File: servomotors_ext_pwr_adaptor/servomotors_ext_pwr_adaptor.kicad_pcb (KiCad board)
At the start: 2 copper layers, 2 parts

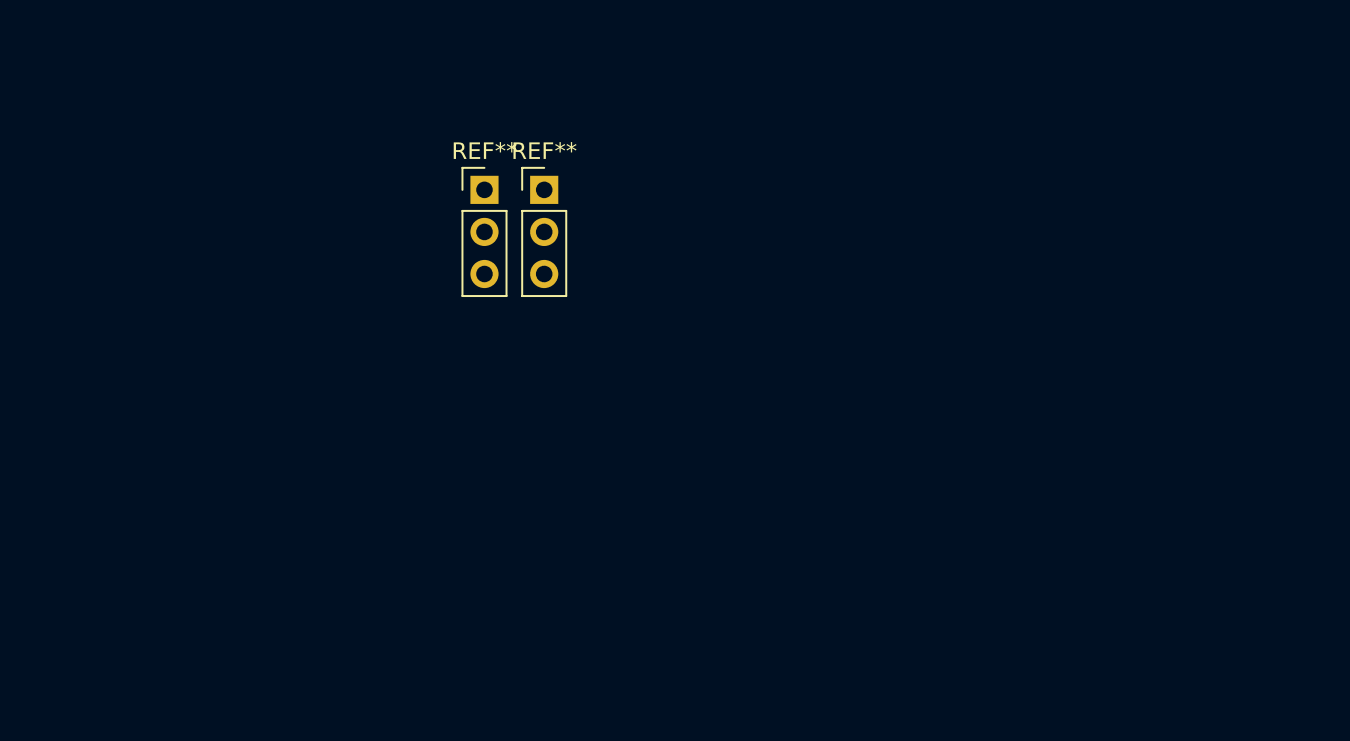
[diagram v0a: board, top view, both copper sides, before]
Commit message: Schematic done. Symbols and footrpints added
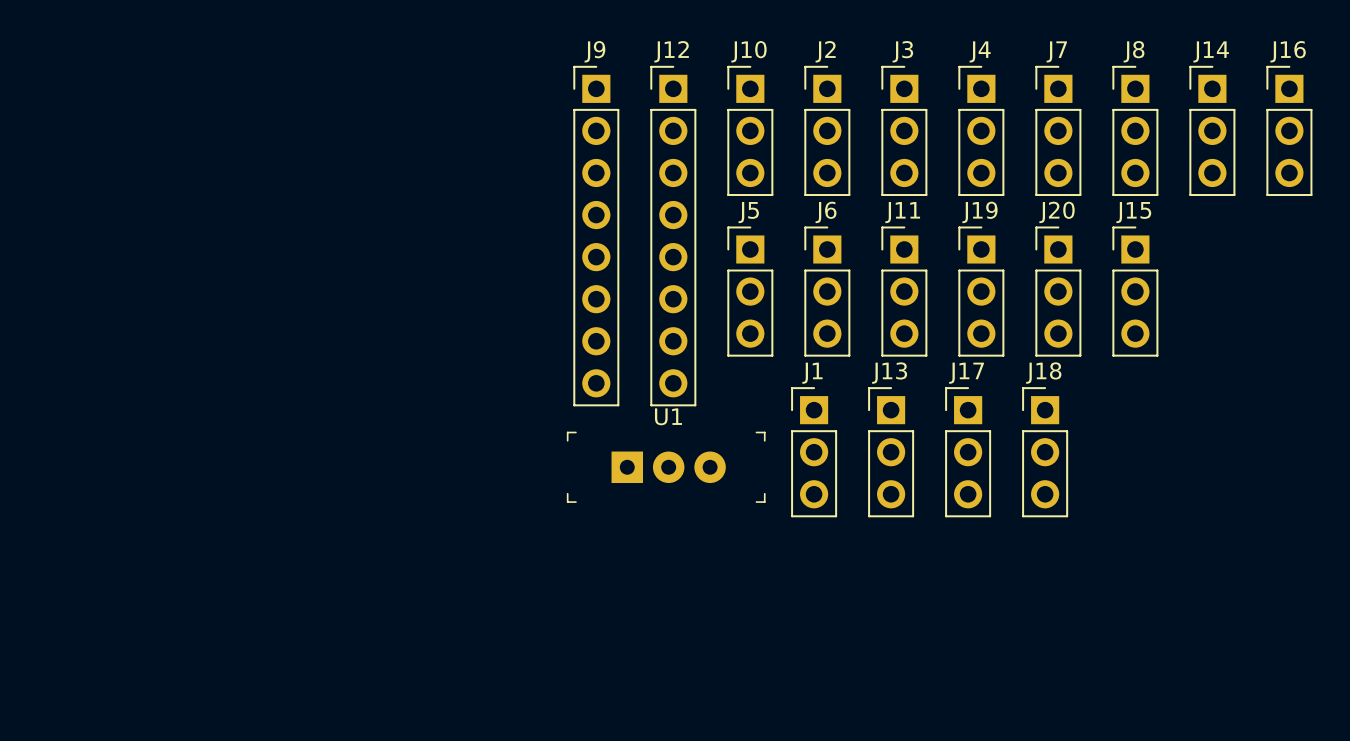
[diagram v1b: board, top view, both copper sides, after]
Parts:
- removed REF** (x2): PinHeader_1x03_P2.54mm_Vertical, Connector_PinHeader_2.54mm:PinHeader_1x03_P2.54mm_Vertical
- added J1: Conn_01x03_Male, Connector_PinHeader_2.54mm:PinHeader_1x03_P2.54mm_Vertical, F.Cu at (138.2, 96.4)
- added J10: Conn_01x03_Male, Connector_PinHeader_2.54mm:PinHeader_1x03_P2.54mm_Vertical, F.Cu at (134.4, 77.0)
- added J11: Conn_01x01_Male, Connector_PinHeader_2.54mm:PinHeader_1x03_P2.54mm_Vertical, F.Cu at (143.7, 86.7)
- added J12: Conn_01x08_Male, Connector_PinHeader_2.54mm:PinHeader_1x08_P2.54mm_Vertical, F.Cu at (129.7, 77.0)
- added J13: Conn_01x03_Male, Connector_PinHeader_2.54mm:PinHeader_1x03_P2.54mm_Vertical, F.Cu at (142.9, 96.4)
- added J14: Conn_01x03_Male, Connector_PinHeader_2.54mm:PinHeader_1x03_P2.54mm_Vertical, F.Cu at (162.3, 77.0)
- added J15: Conn_01x03_Male, Connector_PinHeader_2.54mm:PinHeader_1x03_P2.54mm_Vertical, F.Cu at (157.6, 86.7)
- added J16: Conn_01x03_Male, Connector_PinHeader_2.54mm:PinHeader_1x03_P2.54mm_Vertical, F.Cu at (166.9, 77.0)
- added J17: Conn_01x03_Male, Connector_PinHeader_2.54mm:PinHeader_1x03_P2.54mm_Vertical, F.Cu at (147.5, 96.4)
- added J18: Conn_01x03_Male, Connector_PinHeader_2.54mm:PinHeader_1x03_P2.54mm_Vertical, F.Cu at (152.2, 96.4)
- added J19: Conn_01x03_Male, Connector_PinHeader_2.54mm:PinHeader_1x03_P2.54mm_Vertical, F.Cu at (148.3, 86.7)
- added J2: Conn_01x03_Male, Connector_PinHeader_2.54mm:PinHeader_1x03_P2.54mm_Vertical, F.Cu at (139.0, 77.0)
- added J20: Conn_01x03_Male, Connector_PinHeader_2.54mm:PinHeader_1x03_P2.54mm_Vertical, F.Cu at (153.0, 86.7)
- added J3: Conn_01x03_Male, Connector_PinHeader_2.54mm:PinHeader_1x03_P2.54mm_Vertical, F.Cu at (143.7, 77.0)
- added J4: Conn_01x03_Male, Connector_PinHeader_2.54mm:PinHeader_1x03_P2.54mm_Vertical, F.Cu at (148.3, 77.0)
- added J5: Conn_01x03_Male, Connector_PinHeader_2.54mm:PinHeader_1x03_P2.54mm_Vertical, F.Cu at (134.4, 86.7)
- added J6: Conn_01x03_Male, Connector_PinHeader_2.54mm:PinHeader_1x03_P2.54mm_Vertical, F.Cu at (139.0, 86.7)
- added J7: Conn_01x03_Male, Connector_PinHeader_2.54mm:PinHeader_1x03_P2.54mm_Vertical, F.Cu at (153.0, 77.0)
- added J8: Conn_01x03_Male, Connector_PinHeader_2.54mm:PinHeader_1x03_P2.54mm_Vertical, F.Cu at (157.6, 77.0)
- added J9: Conn_01x08_Male, Connector_PinHeader_2.54mm:PinHeader_1x08_P2.54mm_Vertical, F.Cu at (125.1, 77.0)
- added U1: SW_DPDT_X2, kicad-jcarolinares:Switch_Slide_11.6x4mm_EG1218, F.Cu at (126.9, 99.8)

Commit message: WIP PCB Almost done
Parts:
- removed J1, J10, J13, J14, J15, J16, J17, J18, J19, J2, J20, J3, J4, J5, J6, J7, J8: Conn_01x03_Male, Connector_PinHeader_2.54mm:PinHeader_1x03_P2.54mm_Vertical
- removed J11: Conn_01x01_Male, Connector_PinHeader_2.54mm:PinHeader_1x03_P2.54mm_Vertical
- removed J12: Conn_01x08_Male, Connector_PinHeader_2.54mm:PinHeader_1x08_P2.54mm_Vertical
- removed U1: SW_DPDT_X2, kicad-jcarolinares:Switch_Slide_11.6x4mm_EG1218
- added 1: Conn_01x03_Male, Connector_PinHeader_2.54mm:PinHeader_1x03_P2.54mm_Vertical, F.Cu at (100.1, 87.4)
- added 10: Conn_01x03_Male, Connector_PinHeader_2.54mm:PinHeader_1x03_P2.54mm_Vertical, F.Cu at (102.7, 111.3)
- added 11: Conn_01x03_Male, Connector_PinHeader_2.54mm:PinHeader_1x03_P2.54mm_Vertical, F.Cu at (105.2, 111.3)
- added 12: Conn_01x03_Male, Connector_PinHeader_2.54mm:PinHeader_1x03_P2.54mm_Vertical, F.Cu at (107.7, 111.3)
- added 13: Conn_01x03_Male, Connector_PinHeader_2.54mm:PinHeader_1x03_P2.54mm_Vertical, F.Cu at (110.3, 111.3)
- added 14: Conn_01x03_Male, Connector_PinHeader_2.54mm:PinHeader_1x03_P2.54mm_Vertical, F.Cu at (112.8, 111.3)
- added 15: Conn_01x03_Male, Connector_PinHeader_2.54mm:PinHeader_1x03_P2.54mm_Vertical, F.Cu at (115.4, 111.3)
- added 16: Conn_01x03_Male, Connector_PinHeader_2.54mm:PinHeader_1x03_P2.54mm_Vertical, F.Cu at (117.9, 111.3)
- added 2: Conn_01x03_Male, Connector_PinHeader_2.54mm:PinHeader_1x03_P2.54mm_Vertical, F.Cu at (102.7, 87.4)
- added 3: Conn_01x03_Male, Connector_PinHeader_2.54mm:PinHeader_1x03_P2.54mm_Vertical, F.Cu at (105.2, 87.4)
- added 4: Conn_01x03_Male, Connector_PinHeader_2.54mm:PinHeader_1x03_P2.54mm_Vertical, F.Cu at (107.7, 87.4)
- added 5: Conn_01x03_Male, Connector_PinHeader_2.54mm:PinHeader_1x03_P2.54mm_Vertical, F.Cu at (110.3, 87.4)
- added 6: Conn_01x03_Male, Connector_PinHeader_2.54mm:PinHeader_1x03_P2.54mm_Vertical, F.Cu at (112.8, 87.4)
- added 7: Conn_01x03_Male, Connector_PinHeader_2.54mm:PinHeader_1x03_P2.54mm_Vertical, F.Cu at (115.4, 87.4)
- added 8: Conn_01x03_Male, Connector_PinHeader_2.54mm:PinHeader_1x03_P2.54mm_Vertical, F.Cu at (117.9, 87.4)
- added 8-15: Conn_01x08_Male, Connector_PinHeader_2.54mm:PinHeader_1x08_P2.54mm_Vertical, F.Cu at (100.1, 100.6)
- added 9: Conn_01x03_Male, Connector_PinHeader_2.54mm:PinHeader_1x03_P2.54mm_Vertical, F.Cu at (100.1, 111.3)
- added G: GND to Board, Connector_PinSocket_2.54mm:PinSocket_1x01_P2.54mm_Vertical, F.Cu at (122.3, 87.4)
- added ON: SW_DPDT_X2, kicad-jcarolinares:Switch_Slide_11.6x4mm_EG1218, F.Cu at (122.3, 94.0)
- added PWR: UBEC Connector, Connector_PinHeader_2.54mm:PinHeader_1x03_P2.54mm_Vertical, F.Cu at (122.3, 111.2)
- moved J9 32.7 mm to (100.1, 98.1), turned to 90 degrees
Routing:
- net +5V: track 0.00 -> 15.5 mm
- net S8: track 0.00 -> 5.56 mm
- net S7: track 0.00 -> 5.56 mm
- net S6: track 0.00 -> 5.56 mm
- net S5: track 0.00 -> 5.56 mm
- net S4: track 0.00 -> 5.56 mm
- net S3: track 0.00 -> 5.56 mm
- net S2: track 0.00 -> 5.56 mm
- net S1: track 0.00 -> 5.56 mm
- net S0: track 0.00 -> 5.56 mm
- net S9: track 0.00 -> 5.54 mm
- net S15: track 0.00 -> 5.54 mm
- net S14: track 0.00 -> 5.54 mm
- net S13: track 0.00 -> 5.54 mm
- net S12: track 0.00 -> 5.54 mm
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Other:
- board outline added: 30.5 x 30 mm
- board text added: "G"
- board text added: "V"

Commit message: PCB done. Ready for QA and Gerber files
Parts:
- removed 1, 10: Conn_01x03_Male, Connector_PinHeader_2.54mm:PinHeader_1x03_P2.54mm_Vertical
- added D1: GREEN, LED_THT:LED_D3.0mm, F.Cu at (95.1, 100.6)
- added J1: Conn_01x03_Male, Connector_PinHeader_2.54mm:PinHeader_1x03_P2.54mm_Vertical, F.Cu at (100.1, 87.4)
- added J14: Conn_01x03_Male, Connector_PinHeader_2.54mm:PinHeader_1x03_P2.54mm_Vertical, F.Cu at (102.7, 111.3)
- added J21: 5V to VCC, Connector_PinHeader_2.54mm:PinHeader_1x02_P2.54mm_Vertical, F.Cu at (127.2, 90.0)
- added R1: 1M, Resistor_THT:R_Axial_DIN0207_L6.3mm_D2.5mm_P7.62mm_Horizontal, F.Cu at (126.8, 101.8)
- added R2: 180, Resistor_THT:R_Axial_DIN0207_L6.3mm_D2.5mm_P7.62mm_Horizontal, F.Cu at (95.1, 87.4)
- added U2: DMP3098L-7, kicad-jcarolinares:SOT95P240X110-3N, B.Cu at (126.2, 97.5)
- renumbered PWR to J10, G to J11, 8-15 to J12, 9 to J13, 11 to J15, 12 to J16, 13 to J17, 14 to J18, 15 to J19, 2 to J2, 16 to J20, 3 to J3, 4 to J4, 5 to J5, 6 to J6, 7 to J7, 8 to J8, ON to U1
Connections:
- U1 pad 3: VCC -> Net-(R1-Pad1)
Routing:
- net +5V: track 15.5 -> 26.0 mm
- net Net-(R1-Pad1): track 0.00 -> 9.93 mm
- net Net-(D1-Pad2): track 0.00 -> 3.00 mm
- net VCC: track 0.00 -> 1.57 mm, vias 0 -> 1
- added copper zone on B.Cu, net GND
- added copper zone on F.Cu, net VCC
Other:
- board size 30.5 x 30 mm -> 41 x 30 mm
- board text added: "ON"

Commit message: Simple version done. Prepared for QA and Gerber files
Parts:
- removed D1: GREEN, LED_THT:LED_D3.0mm
- removed R1: 1M, Resistor_THT:R_Axial_DIN0207_L6.3mm_D2.5mm_P7.62mm_Horizontal
- removed R2: 180, Resistor_THT:R_Axial_DIN0207_L6.3mm_D2.5mm_P7.62mm_Horizontal
- removed U1: SW_DPDT_X2, kicad-jcarolinares:Switch_Slide_11.6x4mm_EG1218
- removed U2: DMP3098L-7, kicad-jcarolinares:SOT95P240X110-3N
- moved J21 11.6 mm to (122.3, 100.6)
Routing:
- net +5V: track 26.0 -> 10.3 mm
- net Net-(R1-Pad1): track 9.93 -> 0.00 mm
- net Net-(D1-Pad2): track 3.00 -> 0.00 mm
- net VCC: track 1.57 -> 0.00 mm, vias 1 -> 0
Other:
- board size 41 x 30 mm -> 31.5 x 30 mm
- board text added: "PWD"
- board text removed: "ON"
